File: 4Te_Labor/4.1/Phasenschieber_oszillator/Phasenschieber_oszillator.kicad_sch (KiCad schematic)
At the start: 13 parts, among them U1 TL072

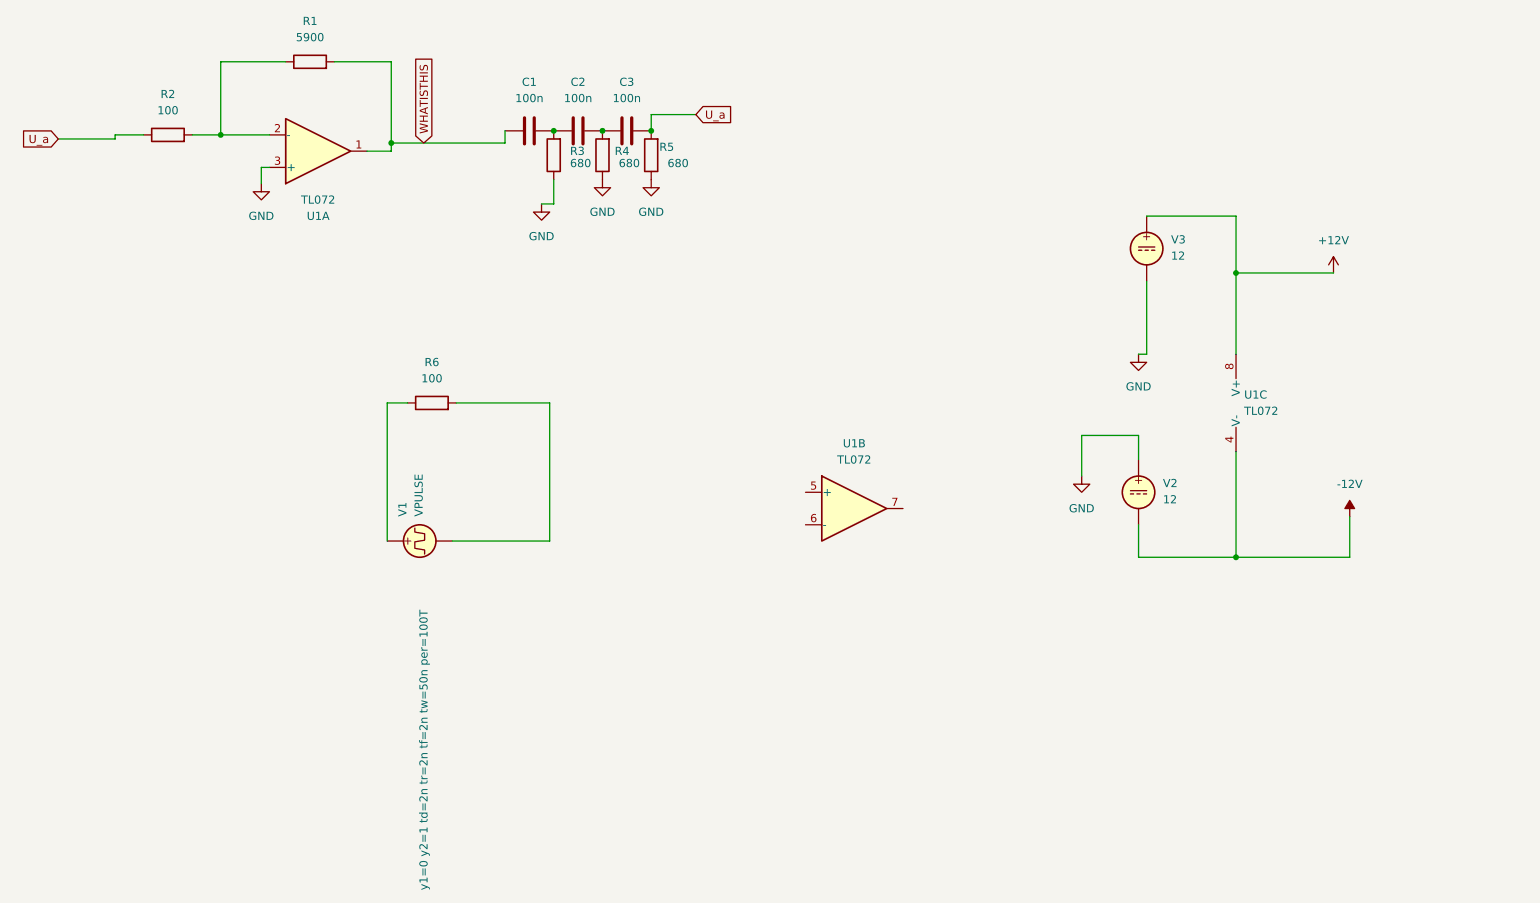
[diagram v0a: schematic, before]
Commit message: Phasenschieberoszillator simuliert
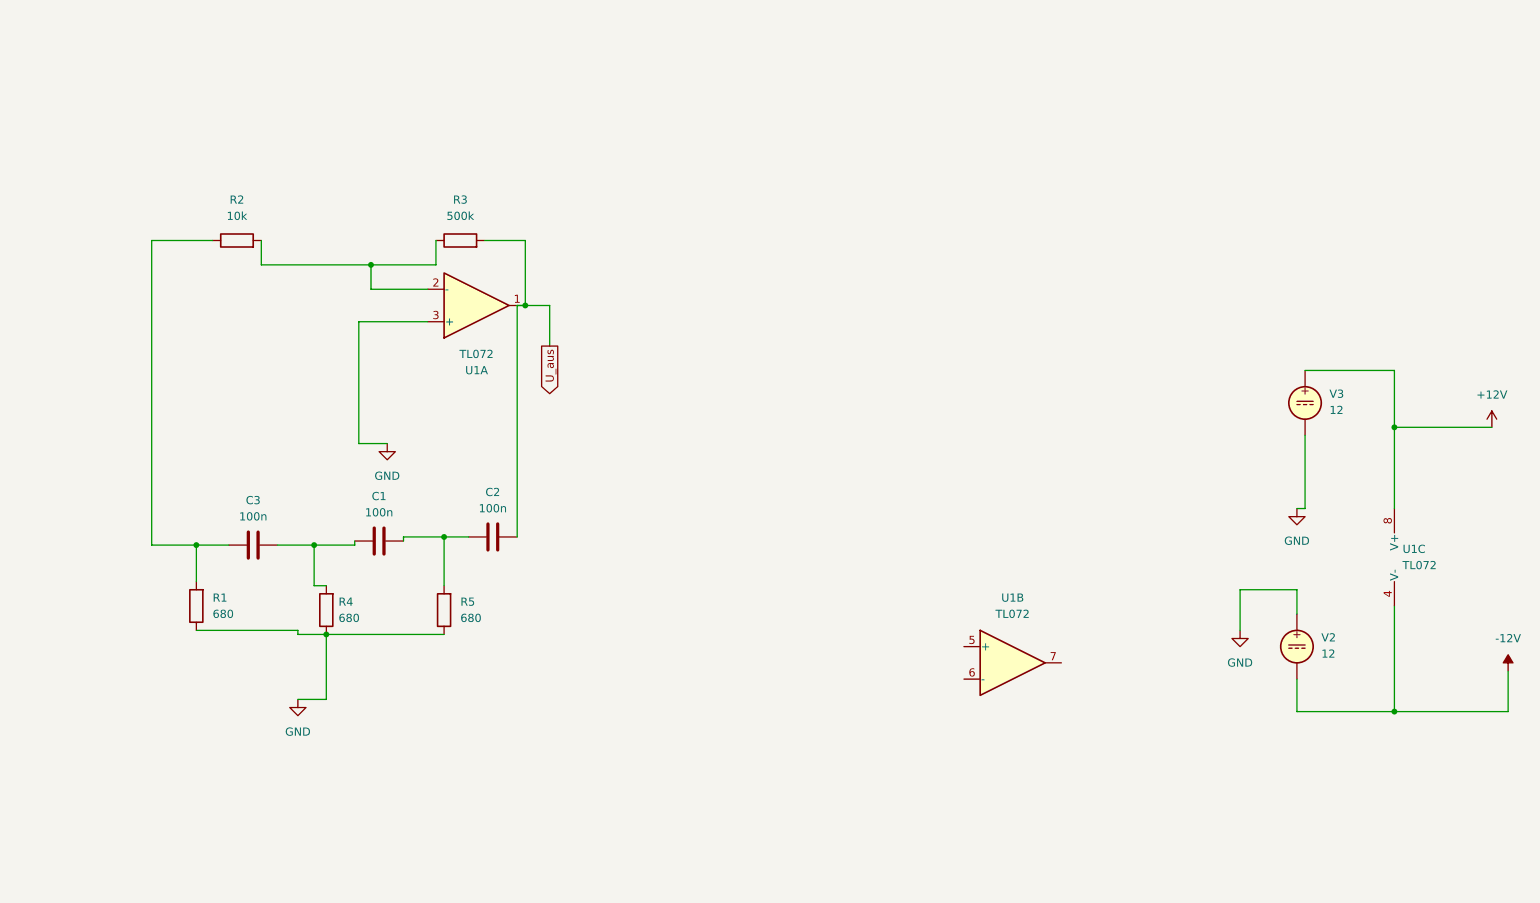
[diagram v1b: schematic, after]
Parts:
- removed R6: 100, symbol Device:R
- removed V1: VPULSE, symbol Simulation_SPICE:VPULSE
- R1: value 5900 -> 680
- R2: value 100 -> 10k
- R3: value 680 -> 500k
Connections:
- net GND: now also R1.1; no longer R3.1
- net at R2.2, U1.2 (-): now also R3.1; no longer R1.1
- net at C3.2, R4.2: now also C1.1; no longer C2.1
- net U_aus: now reaches C2.2, R3.2
- net U_aus: now also U1.1; no longer C1.1
- net U_a: no longer names the net of C3.1, R2.1
- net U_a: now also R1.2; no longer R5.2
- removed net WHATISTHIS: C1.2, R1.2, U1.1
- new net: C1.2, C2.1, R5.2

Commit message: Update code plot
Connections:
- net U_aus renamed U_a
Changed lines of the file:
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@@
     (stroke (width 0) (type default))
   )
-  (global_label "U_aus" (shape output) (at 120.015 72.39 270) (fields_autoplaced)
+  (global_label "U_a" (shape output) (at 120.015 72.39 270) (fields_autoplaced)
     (effects (font (size 1.27 1.27)) (justify right))
-    (property "Intersheetrefs" "${INTERSHEET_REFS}" (at 120.015 80.9994 90)
+    (property "Intersheetrefs" "${INTERSHEET_REFS}" (at 120.015 78.8223 90)
       (effects (font (size 1.27 1.27)) (justify right) hide)
     )
